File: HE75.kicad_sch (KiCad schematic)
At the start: 278 parts, among them J1 USB_C_Receptacle_USB2.0_16P, SW1 Esc, SW10 9, SW11 0, SW12 -, SW13 =, SW14 Bksp, SW15 Del, SW16 Tab, SW17 Q, SW18 W, SW19 E, SW2 1, SW20 R, SW21 T, SW22 Y, SW23 U, SW24 I, SW25 O, SW26 P, SW27 [, SW28 ], SW29 \, SW3 2, SW30 Pg Up, SW31 Caps, SW32 A, SW33 S, SW34 D, SW35 F, SW36 G, SW37 H, SW38 J, SW39 K, SW4 3, SW40 L, SW41 ;, SW42 ', SW43 Enter, SW44 Home, SW45 End, SW46 Shift, SW47 Z, SW48 X, SW49 C, SW5 4, SW50 V, SW51 B, SW52 N, SW53 M, SW54 ,, SW55 ., SW56 /, SW57 Shift, SW58 Code, SW59 Up, SW6 5, SW60 Pg Dn, SW61 Fn, SW62 Ctrl, SW63 Win, SW64 Alt, SW65 Space, SW66 Space, SW67 Space, SW68 Space, SW69 Alt, SW7 6, SW70 Win, SW71 Ctrl, SW72 Fn, SW73 Left, SW74 Down, SW75 Right, SW76 L2U, SW77 C2U/6U, SW78 R2U, SW8 7, SW9 8, U1 STM32F303CCT6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

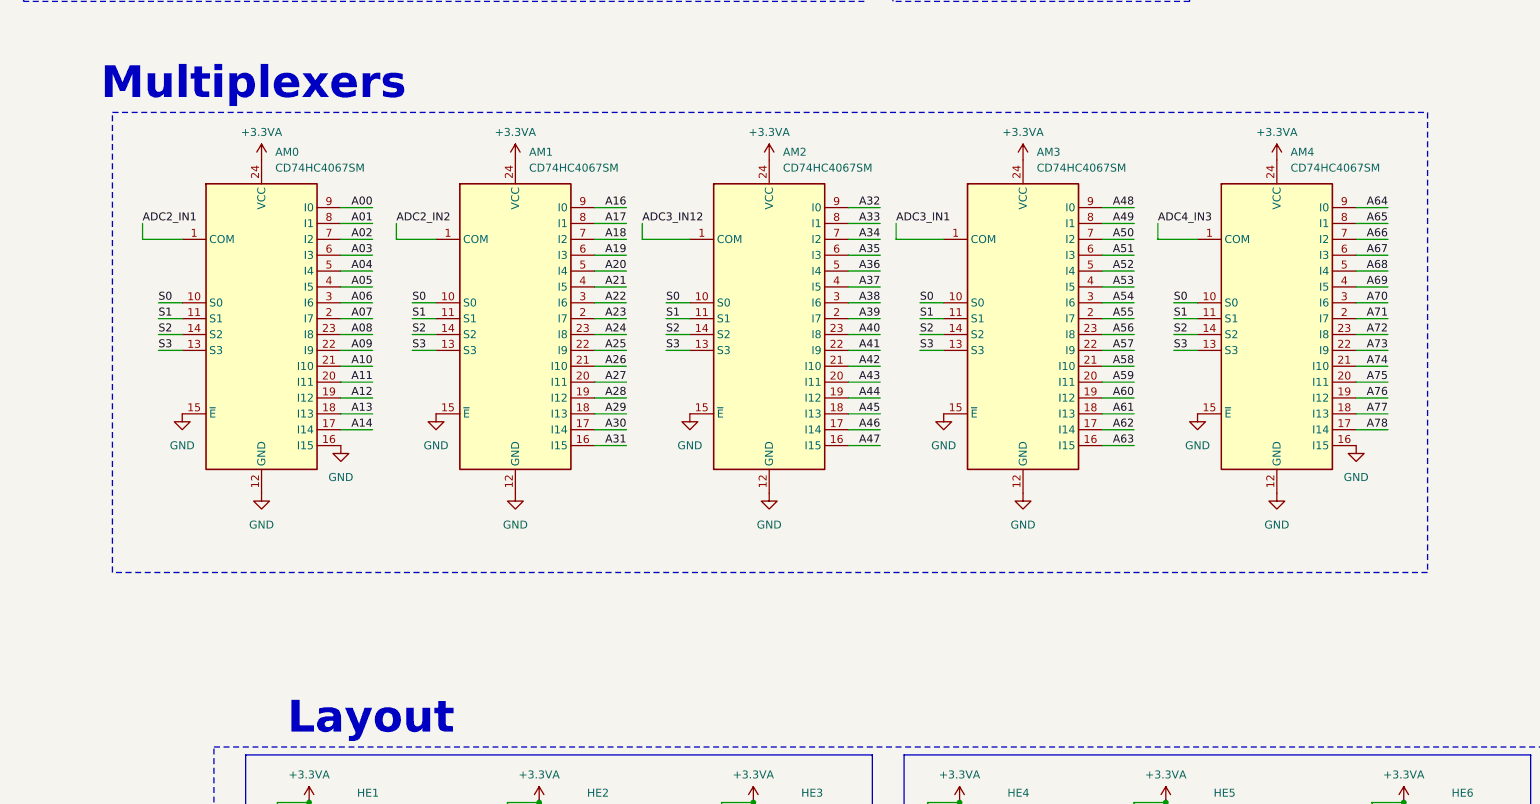
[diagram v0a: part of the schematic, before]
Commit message: Add decoupling capacitors to analog multiplexers
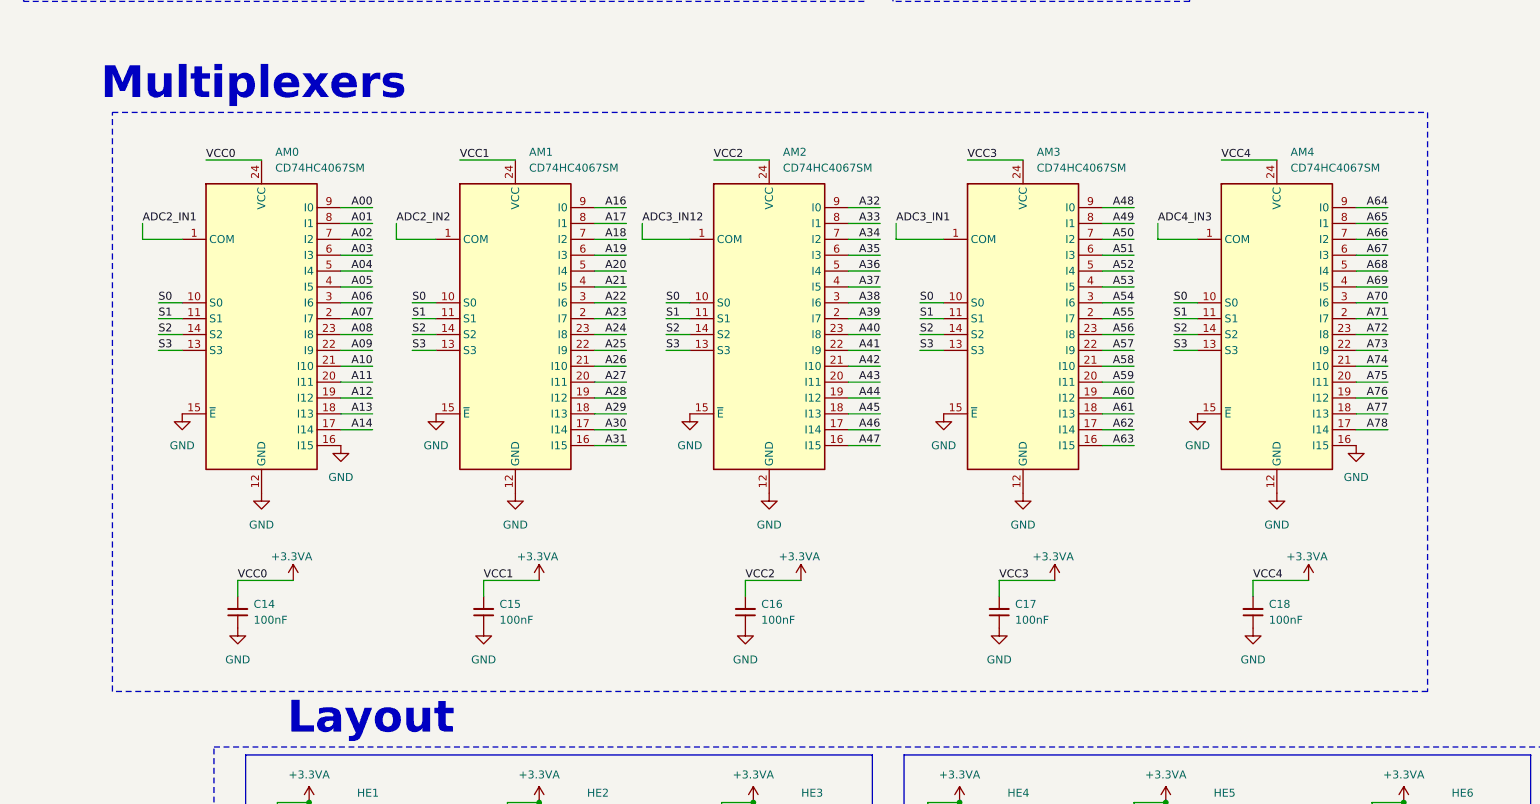
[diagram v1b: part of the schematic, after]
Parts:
- added C14, C15, C16, C17, C18: 100nF, Library:Capacitor 0402, symbol Device:C_Small
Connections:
- net +3.3VA: now also C14.2, C15.2, C16.2, C17.2, C18.2
- net GND: now also C14.1, C15.1, C16.1, C17.1, C18.1

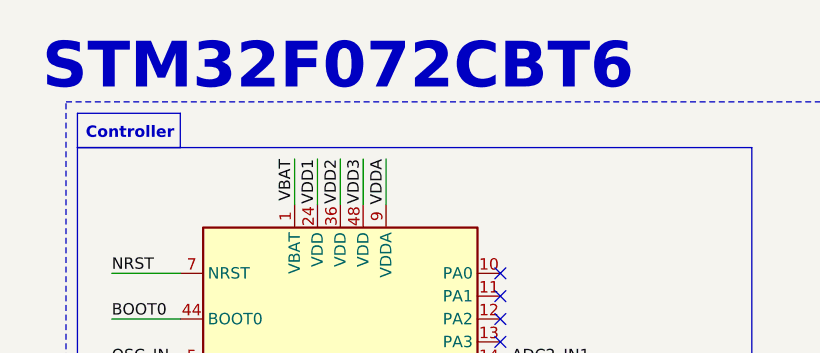
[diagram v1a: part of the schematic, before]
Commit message: Rename schematic section
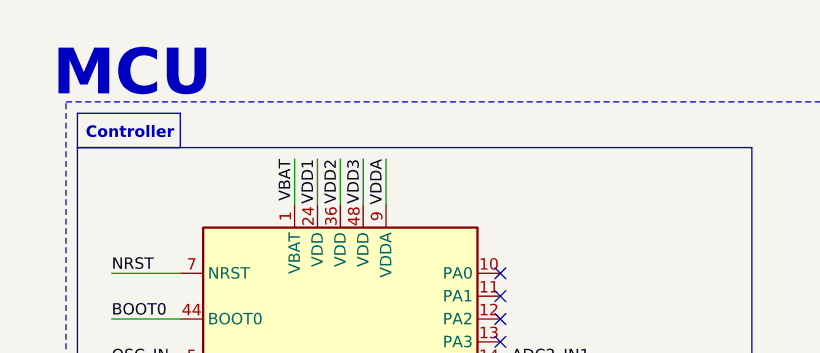
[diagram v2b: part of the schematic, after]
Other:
- note added: "MCU"
- note removed: "STM32F072CBT6"
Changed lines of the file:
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@@
 		)
 	)
-	(text "STM32F072CBT6"
+	(text "MCU"
 		(exclude_from_sim no)
-		(at 46.736 17.78 0)
+		(at 23.876 18.542 0)
 		(effects
 			(font
